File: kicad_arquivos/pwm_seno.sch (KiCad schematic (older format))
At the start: 24 parts, among them J1 PWR, J2 CTRL, Q1 BC337, Q2 BC337, Q3 BC337, Q4 BC337, Q5 IRF9540N, Q6 IRF540N, Q7 IRF9540N, Q8 IRF540N

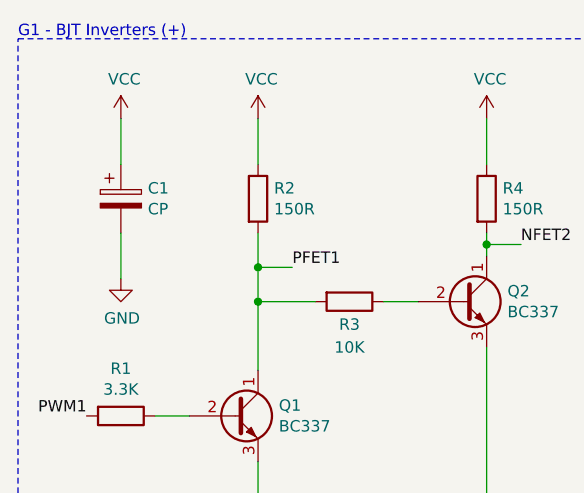
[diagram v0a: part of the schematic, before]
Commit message: Modificado nome da pasta, footprints adicionadas e netlist gerada.
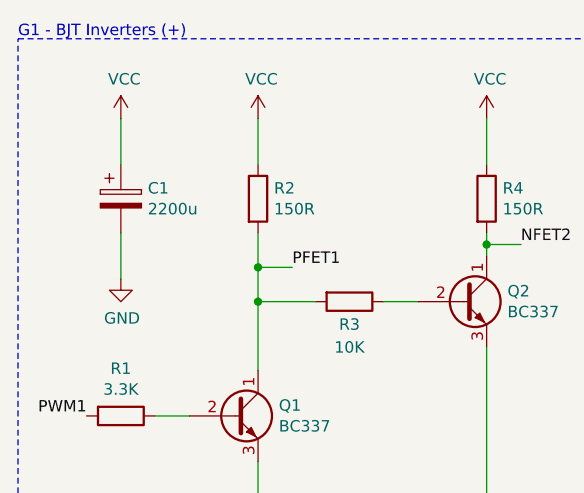
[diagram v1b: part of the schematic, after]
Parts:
- C1: value CP -> 2200u; footprint (none) -> Capacitor_THT:CP_Radial_D24.0mm_P10.00mm_SnapIn
- C2, C3: footprint (none) -> Capacitor_THT:CP_Radial_D24.0mm_P10.00mm_SnapIn
- C4: footprint (none) -> Capacitor_THT:CP_Radial_D8.0mm_P3.80mm
- J1, LS1: footprint (none) -> TerminalBlock:TerminalBlock_bornier-2_P5.08mm
- J2: footprint (none) -> TerminalBlock:TerminalBlock_bornier-3_P5.08mm
- Q1, Q2, Q3, Q4: footprint Package_TO_SOT_THT:TO-92_Inline -> Package_TO_SOT_THT:TO-92_Inline_Wide
- R1, R3, R5, R7: footprint (none) -> Resistor_THT:R_Axial_DIN0207_L6.3mm_D2.5mm_P10.16mm_Horizontal
- R2, R4, R6, R8: footprint (none) -> Resistor_THT:R_Axial_DIN0414_L11.9mm_D4.5mm_P20.32mm_Horizontal
- R9: footprint (none) -> Resistor_THT:R_Axial_DIN0922_L20.0mm_D9.0mm_P30.48mm_Horizontal
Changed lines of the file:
@@
 F 0 "J1" H 1708 6481 50  0000 C CNN
 F 1 "PWR" H 1708 6390 50  0000 C CNN
-F 2 "" H 1600 6300 50  0001 C CNN
+F 2 "TerminalBlock:TerminalBlock_bornier-2_P5.08mm" H 1600 6300 50  0001 C CNN
 F 3 "~" H 1600 6300 50  0001 C CNN
 	1    1600 6300
@@
 F 0 "R6" H 5120 2846 50  0000 L CNN
 F 1 "150R" H 5120 2755 50  0000 L CNN
-F 2 "" V 4980 2800 50  0001 C CNN
+F 2 "Resistor_THT:R_Axial_DIN0414_L11.9mm_D4.5mm_P20.32mm_Horizontal" V 4980 2800 50  0001 C CNN
 F 3 "~" H 5050 2800 50  0001 C CNN
 	1    5050 2800
@@
 F 0 "R8" H 6120 2846 50  0000 L CNN
 F 1 "150R" H 6120 2755 50  0000 L CNN
-F 2 "" V 5980 2800 50  0001 C CNN
+F 2 "Resistor_THT:R_Axial_DIN0414_L11.9mm_D4.5mm_P20.32mm_Horizontal" V 5980 2800 50  0001 C CNN
 F 3 "~" H 6050 2800 50  0001 C CNN
 	1    6050 2800
@@
 F 0 "R5" V 4243 3750 50  0000 C CNN
 F 1 "3.3K" V 4334 3750 50  0000 C CNN
-F 2 "" V 4380 3750 50  0001 C CNN
+F 2 "Resistor_THT:R_Axial_DIN0207_L6.3mm_D2.5mm_P10.16mm_Horizontal" V 4380 3750 50  0001 C CNN
 F 3 "~" H 4450 3750 50  0001 C CNN
 	1    4450 3750
@@
 F 0 "R9" V 9493 3300 50  0000 C CNN
 F 1 "1R" V 9584 3300 50  0000 C CNN
-F 2 "" V 9630 3300 50  0001 C CNN
+F 2 "Resistor_THT:R_Axial_DIN0922_L20.0mm_D9.0mm_P30.48mm_Horizontal" V 9630 3300 50  0001 C CNN
 F 3 "~" H 9700 3300 50  0001 C CNN
 	1    9700 3300
@@
 F 0 "C2" H 4568 2846 50  0000 L CNN
 F 1 "2200u" H 4568 2755 50  0000 L CNN
-F 2 "" H 4488 2650 50  0001 C CNN
+F 2 "Capacitor_THT:CP_Radial_D24.0mm_P10.00mm_SnapIn" H 4488 2650 50  0001 C CNN
 F 3 "~" H 4450 2800 50  0001 C CNN
 	1    4450 2800
@@
 F 0 "Q3" H 5141 3796 50  0000 L CNN
 F 1 "BC337" H 5141 3705 50  0000 L CNN
-F 2 "Package_TO_SOT_THT:TO-92_Inline" H 5150 3675 50  0001 L CIN
+F 2 "Package_TO_SOT_THT:TO-92_Inline_Wide" H 5150 3675 50  0001 L CIN
 F 3 "https://diotec.com/tl_files/diotec/files/pdf/datasheets/bc337.pdf" H 4950 3750 50  0001 L CNN
 	1    4950 3750
@@
 F 0 "Q4" H 6141 3296 50  0000 L CNN
 F 1 "BC337" H 6141 3205 50  0000 L CNN
-F 2 "Package_TO_SOT_THT:TO-92_Inline" H 6150 3175 50  0001 L CIN
+F 2 "Package_TO_SOT_THT:TO-92_Inline_Wide" H 6150 3175 50  0001 L CIN
 F 3 "https://diotec.com/tl_files/diotec/files/pdf/datasheets/bc337.pdf" H 5950 3250 50  0001 L CNN
 	1    5950 3250
@@
 F 0 "C4" V 10405 3100 50  0000 C CNN
 F 1 "33u" V 10314 3100 50  0000 C CNN
-F 2 "" H 10188 2950 50  0001 C CNN
+F 2 "Capacitor_THT:CP_Radial_D8.0mm_P3.80mm" H 10188 2950 50  0001 C CNN
 F 3 "~" H 10150 3100 50  0001 C CNN
 	1    10150 3100
@@
 F 0 "R2" H 2020 2846 50  0000 L CNN
 F 1 "150R" H 2020 2755 50  0000 L CNN
-F 2 "" V 1880 2800 50  0001 C CNN
+F 2 "Resistor_THT:R_Axial_DIN0414_L11.9mm_D4.5mm_P20.32mm_Horizontal" V 1880 2800 50  0001 C CNN
 F 3 "~" H 1950 2800 50  0001 C CNN
 	1    1950 2800
@@
 F 0 "R4" H 3020 2846 50  0000 L CNN
 F 1 "150R" H 3020 2755 50  0000 L CNN
-F 2 "" V 2880 2800 50  0001 C CNN
+F 2 "Resistor_THT:R_Axial_DIN0414_L11.9mm_D4.5mm_P20.32mm_Horizontal" V 2880 2800 50  0001 C CNN
 F 3 "~" H 2950 2800 50  0001 C CNN
 	1    2950 2800
@@
 P 1350 2800
 F 0 "C1" H 1468 2846 50  0000 L CNN
-F 1 "CP" H 1468 2755 50  0000 L CNN
-F 2 "" H 1388 2650 50  0001 C CNN
+F 1 "2200u" H 1468 2755 50  0000 L CNN
+F 2 "Capacitor_THT:CP_Radial_D24.0mm_P10.00mm_SnapIn" H 1388 2650 50  0001 C CNN
 F 3 "~" H 1350 2800 50  0001 C CNN
 	1    1350 2800
@@
 F 0 "Q2" H 3041 3296 50  0000 L CNN
 F 1 "BC337" H 3041 3205 50  0000 L CNN
-F 2 "Package_TO_SOT_THT:TO-92_Inline" H 3050 3175 50  0001 L CIN
+F 2 "Package_TO_SOT_THT:TO-92_Inline_Wide" H 3050 3175 50  0001 L CIN
 F 3 "https://diotec.com/tl_files/diotec/files/pdf/datasheets/bc337.pdf" H 2850 3250 50  0001 L CNN
 	1    2850 3250
@@
 F 0 "Q1" H 2041 3796 50  0000 L CNN
 F 1 "BC337" H 2041 3705 50  0000 L CNN
-F 2 "Package_TO_SOT_THT:TO-92_Inline" H 2050 3675 50  0001 L CIN
+F 2 "Package_TO_SOT_THT:TO-92_Inline_Wide" H 2050 3675 50  0001 L CIN
 F 3 "https://diotec.com/tl_files/diotec/files/pdf/datasheets/bc337.pdf" H 1850 3750 50  0001 L CNN
 	1    1850 3750
@@
 F 0 "R3" V 2450 3250 50  0000 C CNN
 F 1 "10K" V 2550 3250 50  0000 C CNN
-F 2 "" V 2280 3250 50  0001 C CNN
+F 2 "Resistor_THT:R_Axial_DIN0207_L6.3mm_D2.5mm_P10.16mm_Horizontal" V 2280 3250 50  0001 C CNN
 F 3 "~" H 2350 3250 50  0001 C CNN
 	1    2350 3250
@@
 F 0 "R1" V 1143 3750 50  0000 C CNN
 F 1 "3.3K" V 1234 3750 50  0000 C CNN
-F 2 "" V 1280 3750 50  0001 C CNN
+F 2 "Resistor_THT:R_Axial_DIN0207_L6.3mm_D2.5mm_P10.16mm_Horizontal" V 1280 3750 50  0001 C CNN
 F 3 "~" H 1350 3750 50  0001 C CNN
 	1    1350 3750
@@
 F 0 "C3" H 7100 2700 50  0000 L CNN
 F 1 "2200u" H 7000 2600 50  0000 L CNN
-F 2 "" H 7388 2500 50  0001 C CNN
+F 2 "Capacitor_THT:CP_Radial_D24.0mm_P10.00mm_SnapIn" H 7388 2500 50  0001 C CNN
 F 3 "~" H 7350 2650 50  0001 C CNN
 	1    7350 2650
@@
 F 0 "LS1" V 10117 3780 50  0000 L CNN
 F 1 "Speaker" V 10208 3780 50  0000 L CNN
-F 2 "" H 10200 3400 50  0001 C CNN
+F 2 "TerminalBlock:TerminalBlock_bornier-2_P5.08mm" H 10200 3400 50  0001 C CNN
 F 3 "~" H 10190 3550 50  0001 C CNN
 	1    10200 3600
@@
 F 0 "R7" V 5550 3250 50  0000 C CNN
 F 1 "10K" V 5650 3250 50  0000 C CNN
-F 2 "" V 5380 3250 50  0001 C CNN
+F 2 "Resistor_THT:R_Axial_DIN0207_L6.3mm_D2.5mm_P10.16mm_Horizontal" V 5380 3250 50  0001 C CNN
 F 3 "~" H 5450 3250 50  0001 C CNN
 	1    5450 3250
@@
 F 0 "J2" H 1708 7081 50  0000 C CNN
 F 1 "CTRL" H 1708 6990 50  0000 C CNN
-F 2 "" H 1600 6800 50  0001 C CNN
+F 2 "TerminalBlock:TerminalBlock_bornier-3_P5.08mm" H 1600 6800 50  0001 C CNN
 F 3 "~" H 1600 6800 50  0001 C CNN
 	1    1600 6800

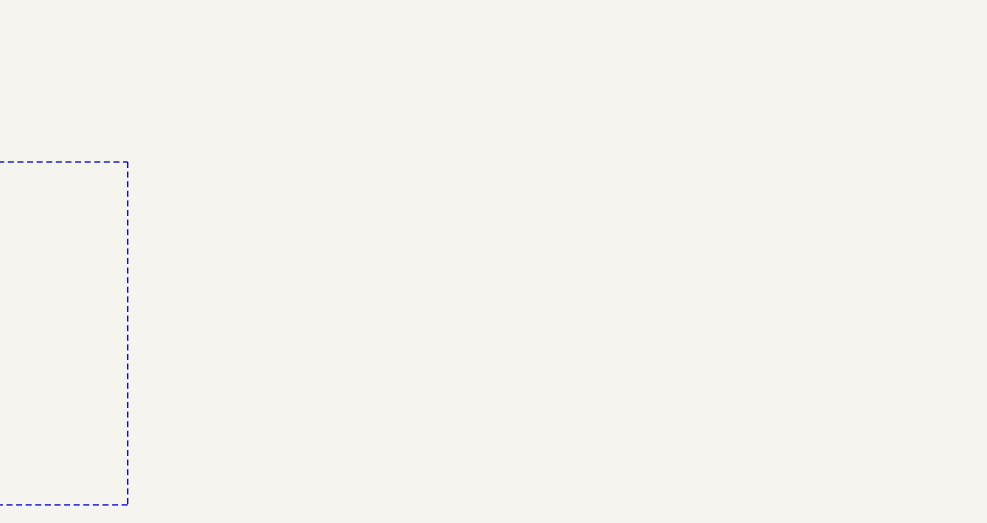
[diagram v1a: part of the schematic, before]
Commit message: Adicionados mounting holes e criado arquivo vazio de PCB
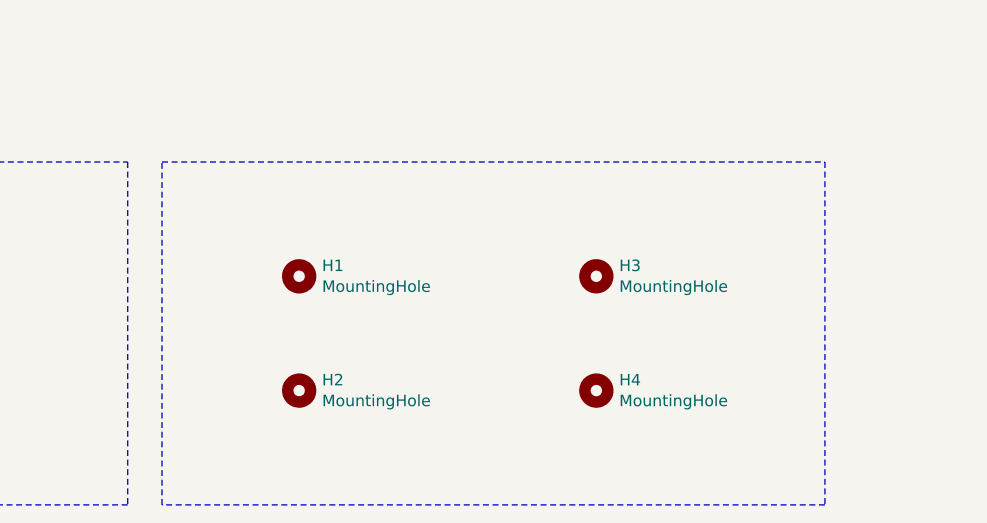
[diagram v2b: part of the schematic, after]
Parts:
- added H1, H2, H3, H4: MountingHole, MountingHole:MountingHole_3.2mm_M3, symbol Mechanical:MountingHole
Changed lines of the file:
@@
 Text Notes 9300 2100 0    50   ~ 0
 G4 - Load and filter
+Wire Notes Line
+	3800 5750 6700 5750
+Wire Notes Line
+	6700 5750 6700 7250
+Wire Notes Line
+	6700 7250 3800 7250
+Wire Notes Line
+	3800 7250 3800 5750
+$Comp
+L Mechanical:MountingHole H1
+U 1 1 5F17BE33
+P 4400 6250
+F 0 "H1" H 4500 6296 50  0000 L CNN
+F 1 "MountingHole" H 4500 6205 50  0000 L CNN
+F 2 "MountingHole:MountingHole_3.2mm_M3" H 4400 6250 50  0001 C CNN
+F 3 "~" H 4400 6250 50  0001 C CNN
+	1    4400 6250
+	1    0    0    -1
+$EndComp
+$Comp
+L Mechanical:MountingHole H2
+U 1 1 5F17C421
+P 4400 6750
+F 0 "H2" H 4500 6796 50  0000 L CNN
+F 1 "MountingHole" H 4500 6705 50  0000 L CNN
+F 2 "MountingHole:MountingHole_3.2mm_M3" H 4400 6750 50  0001 C CNN
+F 3 "~" H 4400 6750 50  0001 C CNN
+	1    4400 6750
+	1    0    0    -1
+$EndComp
+$Comp
+L Mechanical:MountingHole H4
+U 1 1 5F17C5A7
+P 5700 6750
+F 0 "H4" H 5600 6704 50  0000 R CNN
+F 1 "MountingHole" H 5600 6795 50  0000 R CNN
+F 2 "MountingHole:MountingHole_3.2mm_M3" H 5700 6750 50  0001 C CNN
+F 3 "~" H 5700 6750 50  0001 C CNN
+	1    5700 6750
+	-1   0    0    1
+$EndComp
+$Comp
+L Mechanical:MountingHole H3
+U 1 1 5F17C9F5
+P 5700 6250
+F 0 "H3" H 5600 6204 50  0000 R CNN
+F 1 "MountingHole" H 5600 6295 50  0000 R CNN
+F 2 "MountingHole:MountingHole_3.2mm_M3" H 5700 6250 50  0001 C CNN
+F 3 "~" H 5700 6250 50  0001 C CNN
+	1    5700 6250
+	-1   0    0    1
+$EndComp
 $EndSCHEMATC

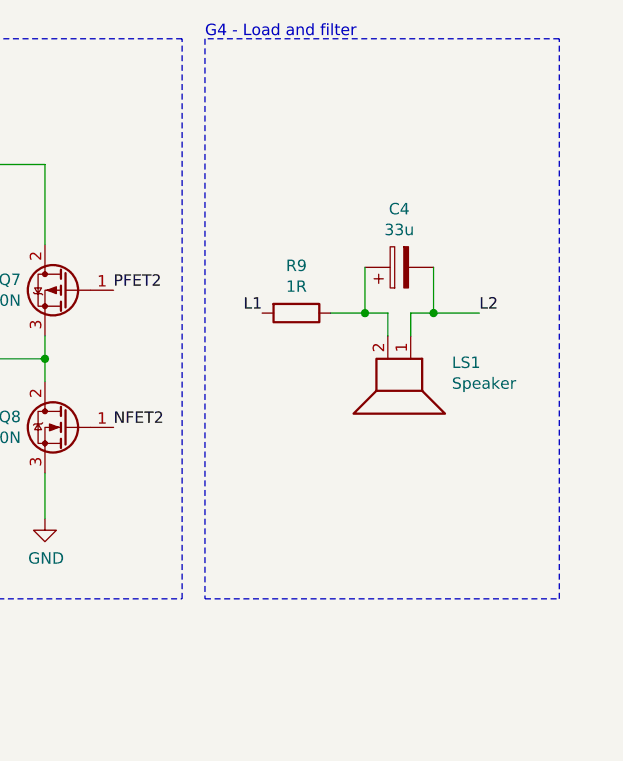
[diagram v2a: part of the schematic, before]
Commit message: Adicionado segundo filtro
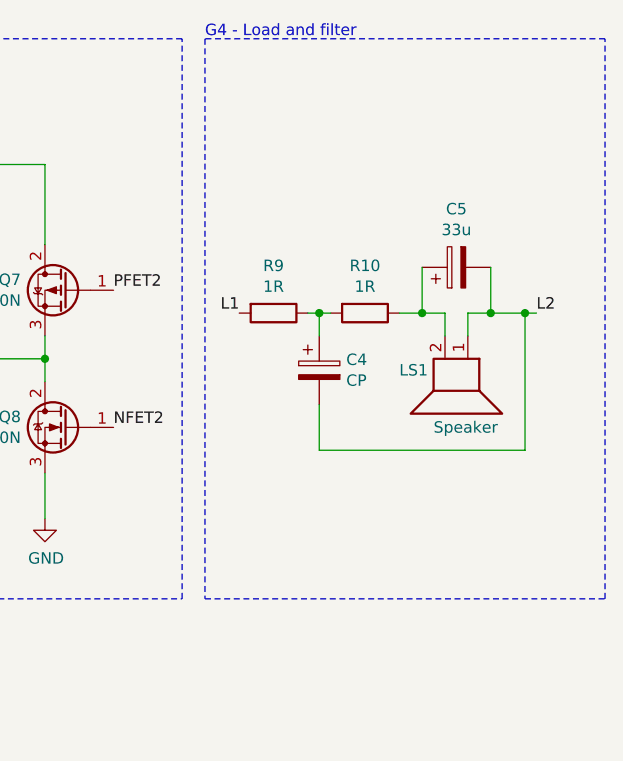
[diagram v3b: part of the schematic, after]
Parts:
- added C4: CP, Capacitor_THT:CP_Radial_D8.0mm_P3.80mm, symbol Device:CP
- added R10: 1R, Resistor_THT:R_Axial_DIN0922_L20.0mm_D9.0mm_P30.48mm_Horizontal, symbol Device:R
- renumbered C4 to C5
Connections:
- net L2: now also C4.2
- net at C5.1, LS1.2: now also R10.1; no longer R9.1
- new net: C4.1, R10.2, R9.1
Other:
- moved on the sheet: C5, LS1, R9
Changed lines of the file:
@@
 L Device:R R9
 U 1 1 5F180E42
-P 9700 3300
-F 0 "R9" V 9493 3300 50  0000 C CNN
-F 1 "1R" V 9584 3300 50  0000 C CNN
-F 2 "Resistor_THT:R_Axial_DIN0922_L20.0mm_D9.0mm_P30.48mm_Horizontal" V 9630 3300 50  0001 C CNN
-F 3 "~" H 9700 3300 50  0001 C CNN
-	1    9700 3300
+P 9600 3300
+F 0 "R9" V 9393 3300 50  0000 C CNN
+F 1 "1R" V 9484 3300 50  0000 C CNN
+F 2 "Resistor_THT:R_Axial_DIN0922_L20.0mm_D9.0mm_P30.48mm_Horizontal" V 9530 3300 50  0001 C CNN
+F 3 "~" H 9600 3300 50  0001 C CNN
+	1    9600 3300
 	0    1    1    0
 $EndComp
@@
 $EndComp
 $Comp
-L Device:CP C4
+L Device:CP C5
 U 1 1 5F18A44B
-P 10150 3100
-F 0 "C4" V 10405 3100 50  0000 C CNN
-F 1 "33u" V 10314 3100 50  0000 C CNN
-F 2 "Capacitor_THT:CP_Radial_D8.0mm_P3.80mm" H 10188 2950 50  0001 C CNN
-F 3 "~" H 10150 3100 50  0001 C CNN
-	1    10150 3100
+P 10400 3100
+F 0 "C5" V 10655 3100 50  0000 C CNN
+F 1 "33u" V 10564 3100 50  0000 C CNN
+F 2 "Capacitor_THT:CP_Radial_D8.0mm_P3.80mm" H 10438 2950 50  0001 C CNN
+F 3 "~" H 10400 3100 50  0001 C CNN
+	1    10400 3100
 	0    -1   -1   0
 $EndComp
 $Comp
-L power:GND #PWR08
+L power:GND #PWR012
 U 1 1 5F193A50
 P 5050 4200
-F 0 "#PWR08" H 5050 3950 50  0001 C CNN
+F 0 "#PWR012" H 5050 3950 50  0001 C CNN
 F 1 "GND" H 5055 4027 50  0000 C CNN
 F 2 "" H 5050 4200 50  0001 C CNN
@@
 $EndComp
 $Comp
-L power:GND #PWR010
+L power:GND #PWR014
 U 1 1 5F193F18
 P 6050 4200
-F 0 "#PWR010" H 6050 3950 50  0001 C CNN
+F 0 "#PWR014" H 6050 3950 50  0001 C CNN
 F 1 "GND" H 6055 4027 50  0000 C CNN
 F 2 "" H 6050 4200 50  0001 C CNN
@@
 $EndComp
 $Comp
-L power:GND #PWR011
+L power:GND #PWR017
 U 1 1 5F1A2636
 P 7600 4200
-F 0 "#PWR011" H 7600 3950 50  0001 C CNN
+F 0 "#PWR017" H 7600 3950 50  0001 C CNN
 F 1 "GND" H 7605 4027 50  0000 C CNN
 F 2 "" H 7600 4200 50  0001 C CNN
@@
 $EndComp
 $Comp
-L power:GND #PWR012
+L power:GND #PWR019
 U 1 1 5F1A2D2F
 P 8600 4200
-F 0 "#PWR012" H 8600 3950 50  0001 C CNN
+F 0 "#PWR019" H 8600 3950 50  0001 C CNN
 F 1 "GND" H 8605 4027 50  0000 C CNN
 F 2 "" H 8600 4200 50  0001 C CNN
@@
 $EndComp
 $Comp
-L power:VCC #PWR09
+L power:VCC #PWR013
 U 1 1 5F1A33DE
 P 6050 2450
-F 0 "#PWR09" H 6050 2300 50  0001 C CNN
+F 0 "#PWR013" H 6050 2300 50  0001 C CNN
 F 1 "VCC" H 6065 2623 50  0000 C CNN
 F 2 "" H 6050 2450 50  0001 C CNN
@@
 $EndComp
 $Comp
-L power:VCC #PWR07
+L power:VCC #PWR011
 U 1 1 5F1A4841
 P 5050 2450
-F 0 "#PWR07" H 5050 2300 50  0001 C CNN
+F 0 "#PWR011" H 5050 2300 50  0001 C CNN
 F 1 "VCC" H 5065 2623 50  0000 C CNN
 F 2 "" H 5050 2450 50  0001 C CNN
@@
 $EndComp
 $Comp
-L power:VCC #PWR05
+L power:VCC #PWR07
 U 1 1 5F1D4C1A
 P 2950 2450
-F 0 "#PWR05" H 2950 2300 50  0001 C CNN
+F 0 "#PWR07" H 2950 2300 50  0001 C CNN
 F 1 "VCC" H 2965 2623 50  0000 C CNN
 F 2 "" H 2950 2450 50  0001 C CNN
@@
 $EndComp
 $Comp
-L power:VCC #PWR01
+L power:VCC #PWR03
 U 1 1 5F1D4C24
 P 1950 2450
-F 0 "#PWR01" H 1950 2300 50  0001 C CNN
+F 0 "#PWR03" H 1950 2300 50  0001 C CNN
 F 1 "VCC" H 1965 2623 50  0000 C CNN
 F 2 "" H 1950 2450 50  0001 C CNN
@@
 $EndComp
 $Comp
-L power:GND #PWR06
+L power:GND #PWR08
 U 1 1 5F1D4C10
 P 2950 4200
-F 0 "#PWR06" H 2950 3950 50  0001 C CNN
+F 0 "#PWR08" H 2950 3950 50  0001 C CNN
 F 1 "GND" H 2955 4027 50  0000 C CNN
 F 2 "" H 2950 4200 50  0001 C CNN
@@
 $EndComp
 $Comp
-L power:GND #PWR02
+L power:GND #PWR04
 U 1 1 5F1D4C06
 P 1950 4200
-F 0 "#PWR02" H 1950 3950 50  0001 C CNN
+F 0 "#PWR04" H 1950 3950 50  0001 C CNN
 F 1 "GND" H 1955 4027 50  0000 C CNN
 F 2 "" H 1950 4200 50  0001 C CNN
@@
 $EndComp
 $Comp
-L power:VCC #PWR03
+L power:VCC #PWR05
 U 1 1 5F206D63
 P 2550 6300
-F 0 "#PWR03" H 2550 6150 50  0001 C CNN
+F 0 "#PWR05" H 2550 6150 50  0001 C CNN
 F 1 "VCC" H 2565 6473 50  0000 C CNN
 F 2 "" H 2550 6300 50  0001 C CNN
@@
 $EndComp
 $Comp
-L power:GND #PWR04
+L power:GND #PWR06
 U 1 1 5F2073C4
 P 2550 6650
-F 0 "#PWR04" H 2550 6400 50  0001 C CNN
+F 0 "#PWR06" H 2550 6400 50  0001 C CNN
 F 1 "GND" H 2555 6477 50  0000 C CNN
 F 2 "" H 2550 6650 50  0001 C CNN
@@
 	1950 2650 1950 2450
 $Comp
-L power:VCC #PWR013
+L power:VCC #PWR01
 U 1 1 5F210C0D
 P 1350 2450
-F 0 "#PWR013" H 1350 2300 50  0001 C CNN
+F 0 "#PWR01" H 1350 2300 50  0001 C CNN
 F 1 "VCC" H 1365 2623 50  0000 C CNN
 F 2 "" H 1350 2450 50  0001 C CNN
@@
 	1350 2650 1350 2450
 $Comp
-L power:GND #PWR014
+L power:GND #PWR02
 U 1 1 5F2111D1
 P 1350 3150
-F 0 "#PWR014" H 1350 2900 50  0001 C CNN
+F 0 "#PWR02" H 1350 2900 50  0001 C CNN
 F 1 "GND" H 1355 2977 50  0000 C CNN
 F 2 "" H 1350 3150 50  0001 C CNN
@@
 	1350 3150 1350 2950
 $Comp
-L power:VCC #PWR015
+L power:VCC #PWR09
 U 1 1 5F21208A
 P 4450 2450
-F 0 "#PWR015" H 4450 2300 50  0001 C CNN
+F 0 "#PWR09" H 4450 2300 50  0001 C CNN
 F 1 "VCC" H 4465 2623 50  0000 C CNN
 F 2 "" H 4450 2450 50  0001 C CNN
@@
 	8600 4000 8600 4200
 $Comp
-L power:VCC #PWR019
+L power:VCC #PWR018
 U 1 1 5F21964C
 P 8100 2450
-F 0 "#PWR019" H 8100 2300 50  0001 C CNN
+F 0 "#PWR018" H 8100 2300 50  0001 C CNN
 F 1 "VCC" H 8115 2623 50  0000 C CNN
 F 2 "" H 8100 2450 50  0001 C CNN
@@
 $EndComp
 $Comp
-L power:VCC #PWR017
+L power:VCC #PWR015
 U 1 1 5F21F7FE
 P 7350 2450
-F 0 "#PWR017" H 7350 2300 50  0001 C CNN
+F 0 "#PWR015" H 7350 2300 50  0001 C CNN
 F 1 "VCC" H 7365 2623 50  0000 C CNN
 F 2 "" H 7350 2450 50  0001 C CNN
@@
 	7350 2450 7350 2500
 $Comp
-L power:GND #PWR018
+L power:GND #PWR016
 U 1 1 5F220309
 P 7350 2850
-F 0 "#PWR018" H 7350 2600 50  0001 C CNN
+F 0 "#PWR016" H 7350 2600 50  0001 C CNN
 F 1 "GND" H 7355 2677 50  0000 C CNN
 F 2 "" H 7350 2850 50  0001 C CNN
@@
 L Device:Speaker LS1
 U 1 1 5F18B602
-P 10200 3600
-F 0 "LS1" V 10117 3780 50  0000 L CNN
-F 1 "Speaker" V 10208 3780 50  0000 L CNN
-F 2 "TerminalBlock:TerminalBlock_bornier-2_P5.08mm" H 10200 3400 50  0001 C CNN
-F 3 "~" H 10190 3550 50  0001 C CNN
-	1    10200 3600
+P 10450 3600
+F 0 "LS1" V 10400 3300 50  0000 L CNN
+F 1 "Speaker" V 10650 3450 50  0000 L CNN
+F 2 "TerminalBlock:TerminalBlock_bornier-2_P5.08mm" H 10450 3400 50  0001 C CNN
+F 3 "~" H 10440 3550 50  0001 C CNN
+	1    10450 3600
 	0    1    1    0
 $EndComp
-Text Label 9550 3300 2    50   ~ 0
+Text Label 9450 3300 2    50   ~ 0
 L1
 Wire Wire Line
-	10200 3400 10200 3300
-Wire Wire Line
-	10200 3300 10300 3300
-Wire Wire Line
-	10300 3300 10300 3100
-Wire Wire Line
-	10300 3300 10500 3300
-Connection ~ 10300 3300
-Wire Wire Line
-	9850 3300 10000 3300
-Wire Wire Line
-	10000 3300 10000 3100
-Wire Wire Line
-	10000 3300 10100 3300
-Wire Wire Line
-	10100 3300 10100 3400
-Connection ~ 10000 3300
-Text Label 10500 3300 0    50   ~ 0
+	10450 3400 10450 3300
+Wire Wire Line
+	10450 3300 10550 3300
+Wire Wire Line
+	10550 3300 10550 3100
+Wire Wire Line
+	10550 3300 10700 3300
+Connection ~ 10550 3300
+Wire Wire Line
+	10250 3300 10250 3100
+Wire Wire Line
+	10250 3300 10350 3300
+Wire Wire Line
+	10350 3300 10350 3400
+Connection ~ 10250 3300
+Text Label 10750 3300 0    50   ~ 0
 L2
 Text Label 2100 3100 0    50   ~ 0
@@
 	4450 2950 4450 3150
 $Comp
-L power:GND #PWR016
+L power:GND #PWR010
 U 1 1 5F2119EB
 P 4450 3150
-F 0 "#PWR016" H 4450 2900 50  0001 C CNN
+F 0 "#PWR010" H 4450 2900 50  0001 C CNN
 F 1 "GND" H 4455 2977 50  0000 C CNN
 F 2 "" H 4450 3150 50  0001 C CNN
@@
 	9200 2100 6800 2100
 Wire Notes Line
-	9300 4550 10850 4550
-Wire Notes Line
-	10850 4550 10850 2100
-Wire Notes Line
-	10850 2100 9300 2100
+	9300 4550 11050 4550
+Wire Notes Line
+	11050 4550 11050 2100
+Wire Notes Line
+	11050 2100 9300 2100
 Wire Notes Line
 	9300 2100 9300 4550
@@
 	-1   0    0    1
 $EndComp
+$Comp
+L Device:CP C4
+U 1 1 5F18BA23
+P 9800 3550
+F 0 "C4" H 9918 3596 50  0000 L CNN
+F 1 "CP" H 9918 3505 50  0000 L CNN
+F 2 "Capacitor_THT:CP_Radial_D8.0mm_P3.80mm" H 9838 3400 50  0001 C CNN
+F 3 "~" H 9800 3550 50  0001 C CNN
+	1    9800 3550
+	1    0    0    -1
+$EndComp
+$Comp
+L Device:R R10
+U 1 1 5F18DF61
+P 10000 3300
+F 0 "R10" V 9793 3300 50  0000 C CNN
+F 1 "1R" V 9884 3300 50  0000 C CNN
+F 2 "Resistor_THT:R_Axial_DIN0922_L20.0mm_D9.0mm_P30.48mm_Horizontal" V 9930 3300 50  0001 C CNN
+F 3 "~" H 10000 3300 50  0001 C CNN
+	1    10000 3300
+	0    1    1    0
+$EndComp
+Wire Wire Line
+	10150 3300 10250 3300
+Wire Wire Line
+	9800 3400 9800 3300
+Wire Wire Line
+	9800 3300 9750 3300
+Wire Wire Line
+	9850 3300 9800 3300
+Connection ~ 9800 3300
+Wire Wire Line
+	9800 3700 9800 3900
+Wire Wire Line
+	9800 3900 10700 3900
+Wire Wire Line
+	10700 3900 10700 3300
+Connection ~ 10700 3300
+Wire Wire Line
+	10700 3300 10750 3300
 $EndSCHEMATC
